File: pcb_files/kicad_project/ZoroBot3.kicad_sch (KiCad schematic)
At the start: 126 parts, among them Q1 NMOS, Q2 AON7423, U1 MPU-6500, Y1 Crystal_GND24

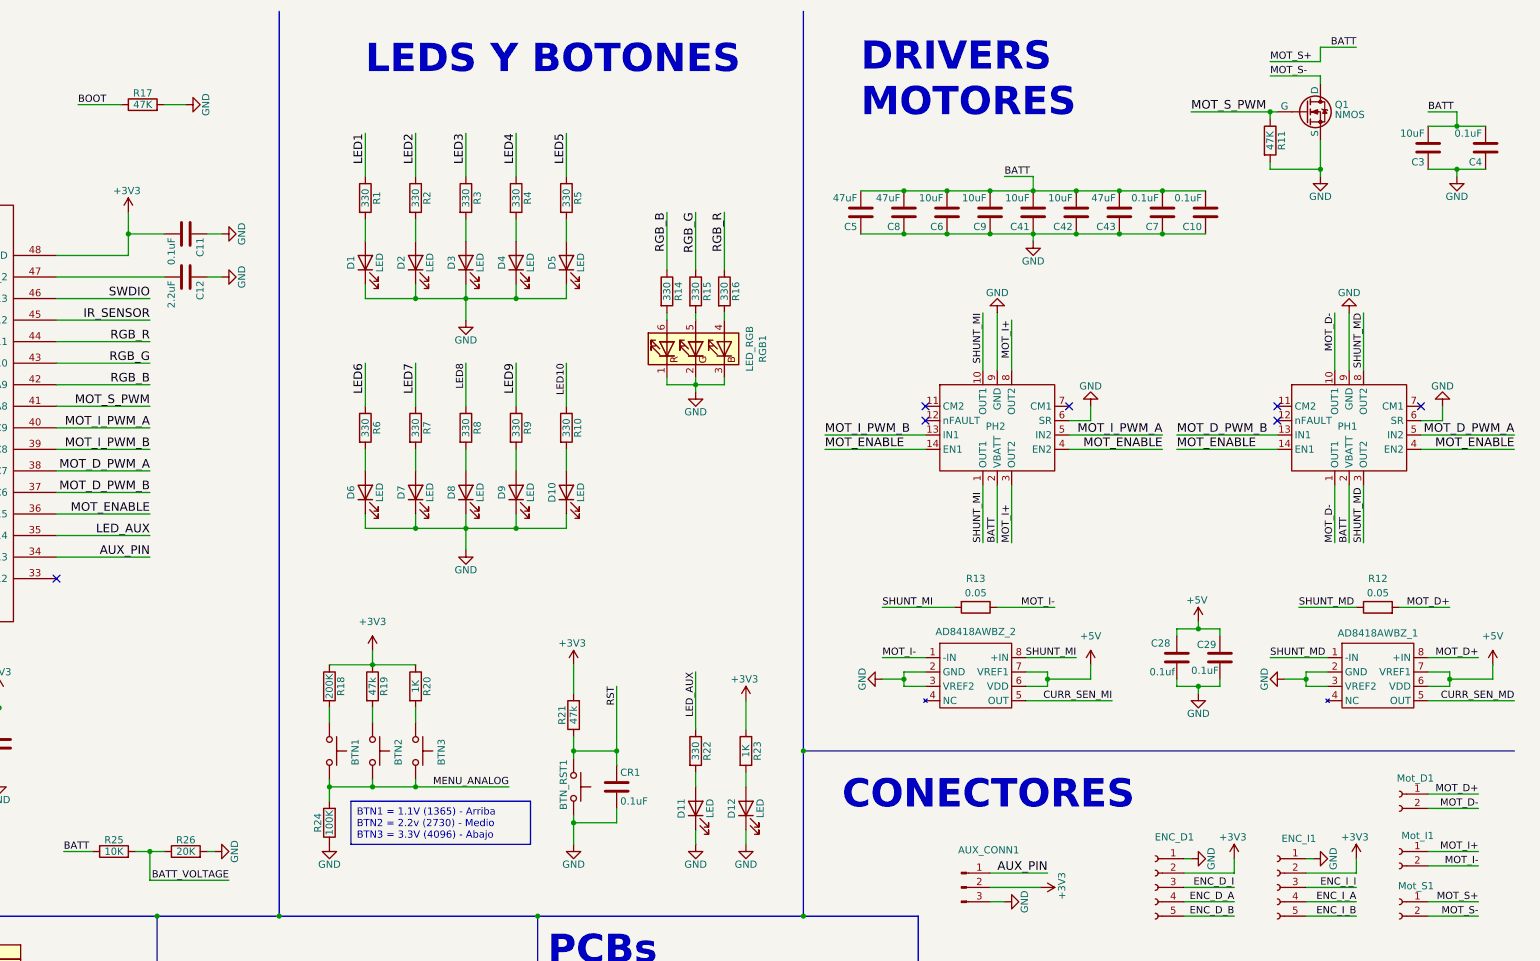
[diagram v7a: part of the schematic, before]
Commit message: Realiza preparativos de la adecuacion del hardware y comentarios en el esquematico
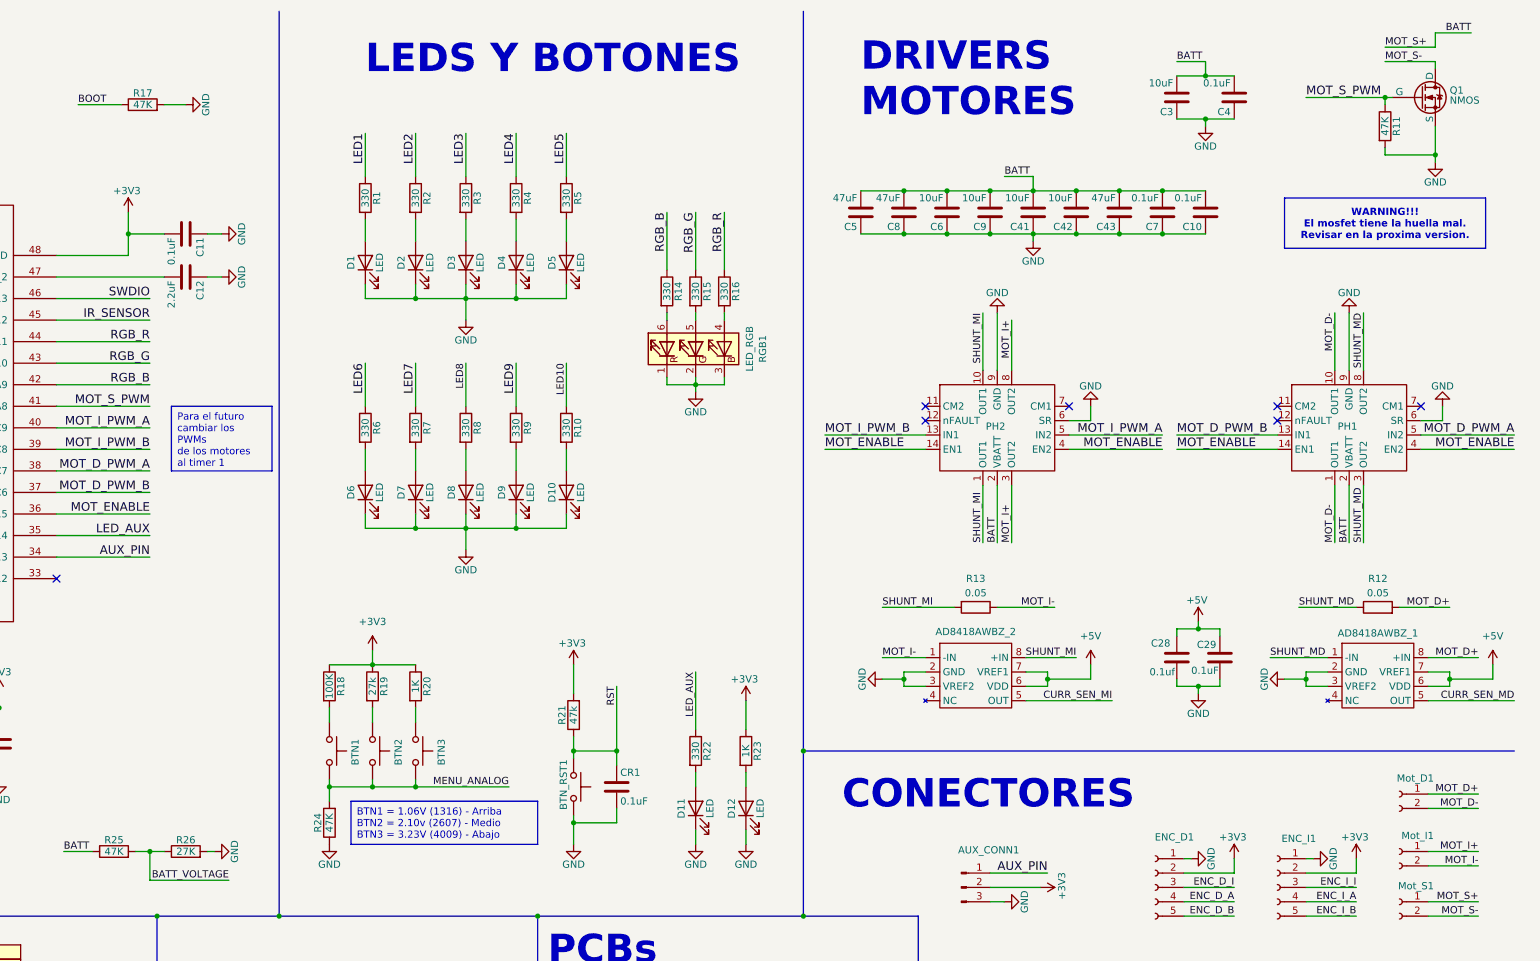
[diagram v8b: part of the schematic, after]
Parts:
- R18: value 200K -> 100K
- R19: value 47k -> 27k
- R24: value 100K -> 47K
- R25: value 10K -> 47K
- R26: value 20K -> 27K
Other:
- moved on the sheet: C3, C4, Q1, R11
